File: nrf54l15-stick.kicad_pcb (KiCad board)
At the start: 4 copper layers, 14.5 x 22.5 mm, 29 parts, among them J1 USB_A, J2 programming conn, J3 Conn_01x04_Pin, SW4 SW_Push, SW5 SW_Push, SW6 Processor_reset, U3 APX803L20-29C3-7, U4 CP2102C-Axx-xQFN24, U5 BM15C, Y1 32.768kHz

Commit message: shrunk, routed, passes drc, no checklist yet
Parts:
- removed C4: 4.7uF/10V, Capacitor_SMD:C_0805_2012Metric
- removed J3: Conn_01x04_Pin, footprint:UART-sot
- removed SW5: SW_Push, footprint:SW_STU-057A23AC_8127_2.25N
- removed SW6: Processor_reset, footprint:SW_STU-057A23AC_8127_2.25N
- added C8: 4.7uF/10V, Capacitor_SMD:C_0603_1608Metric, B.Cu at (110.0, 95.2)
- added FID4: Fiducial, Fiducial:Fiducial_0.5mm_Mask1mm, B.Cu at (112.8, 86.4)
- added FID5: Fiducial, Fiducial:Fiducial_0.5mm_Mask1mm, B.Cu at (100.8, 86.4)
- added FID6: Fiducial, Fiducial:Fiducial_0.5mm_Mask1mm, B.Cu at (112.8, 95.4)
- C16: value 0.10uF/50V/0402 -> 0.10uF/50v
- C20: value 0.10uF/50V/0603 -> 0.10uF/50v; footprint Capacitor_SMD:C_0603_1608Metric -> Capacitor_SMD:C_0402_1005Metric
- C7: footprint Capacitor_SMD:C_0805_2012Metric -> Capacitor_SMD:C_0603_1608Metric
- D7, D8: footprint LED_SMD:LED_0805_2012Metric -> footprint:LED_0805_2012Metric; moved to B.Cu
- FID1, FID2, FID3: footprint Fiducial:Fiducial_1mm_Mask2mm -> Fiducial:Fiducial_0.5mm_Mask1mm
- H2, R16, SW4, Y1: moved to B.Cu
- R15: footprint Capacitor_SMD:C_0603_1608Metric -> Resistor_SMD:R_0603_1608Metric; moved to B.Cu
- R17: value 100K/0603 -> 100K; footprint Resistor_SMD:R_0603_1608Metric -> Resistor_SMD:R_0402_1005Metric
- R29: value 1.00K/0603 -> 1.00K; footprint Resistor_SMD:R_0603_1608Metric -> Resistor_SMD:R_0402_1005Metric
- R7: value 1k/0603 -> 1.00k; footprint Resistor_SMD:R_0603_1608Metric -> Resistor_SMD:R_0402_1005Metric
- R8: value 22.1k/0603 -> 22.1k; footprint Resistor_SMD:R_0603_1608Metric -> Resistor_SMD:R_0402_1005Metric
- R9: value 47.5k/0603 -> 47.5k; footprint Resistor_SMD:R_0603_1608Metric -> Resistor_SMD:R_0402_1005Metric
- U3: value APX803L20-29C3-7 -> APX803L20-27SR-7
- U4: footprint Package_DFN_QFN:WQFN-24-1EP_4x4mm_P0.5mm_EP2.45x2.45mm -> footprint:QFN-24-1EP_4x4mm_P0.5mm_EP2.5x2.5mm
- moved FID2 80.5 mm to (100.8, 93.0)
- moved C20 78.3 mm to (100.8, 92.2), turned to -90 degrees
- moved R17 77.0 mm to (101.8, 92.2), turned to 90 degrees
- moved SW4 74.7 mm to (101.4, 89.2), turned to 90 degrees
- moved U3 73.7 mm to (104.4, 90.8), turned to 180 degrees
- moved Z1 70.5 mm to (104.8, 95.6)
- moved D8 69.2 mm to (105.6, 87.8), turned to 90 degrees
- moved R7 67.9 mm to (102.8, 92.2), turned to 90 degrees
- moved Y1 67.4 mm to (104.8, 93.0)
- moved C16 66.7 mm to (101.6, 95.0)
- moved U5 66.5 mm to (106.8, 86.0)
- moved J2 66.4 mm to (106.8, 84.7)
- moved FID1 66.2 mm to (100.8, 84.6)
- moved R16 66.1 mm to (112.8, 93.0)
- moved R29 65.9 mm to (111.4, 87.2), turned to -90 degrees
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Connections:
- U4 pad 20: /UART_RX -> /UART_nRF_TX
- U4 pad 21: /UART_TX -> /UART_nRF_RX
- U5 pad A3: /P1.09 -> unconnected-(U5-P1.09-PadA3)
- U5 pad B3: /P1.11/AIN4 -> unconnected-(U5-P1.11/AIN4-PadB3)
- U5 pad B4: /P1.12/AIN5 -> unconnected-(U5-P1.12/AIN5-PadB4)
- U5 pad B5: /P1.13/AIN6 -> unconnected-(U5-P1.13/AIN6-PadB5)
- U5 pad B6: /P1.14/AIN7 -> unconnected-(U5-P1.14/AIN7-PadB6)
- U5 pad E8: /I2C_SDA -> unconnected-(U5-P1.03-PadE8)
- U5 pad E9: /I2C_SCL -> unconnected-(U5-P1.04/AIN0-PadE9)
- U5 pad F8: /UART_TX -> /UART_nRF_TX
- U5 pad F9: /UART_RX -> /UART_nRF_RX
- U5 pad G8: /PWM_CH_Y -> unconnected-(U5-P1.08-PadG8)
- U5 pad G9: /PWM_CH_X -> unconnected-(U5-P1.07/AIN3-PadG9)
- U5 pad J2: /BUTTON1 -> unconnected-(U5-P0.03-PadJ2)
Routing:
- net Net-(D8-A): track 2.20 -> 29.8 mm, vias 0 -> 2
- net /UART_RX: track 25.9 -> 0.00 mm, vias 3 -> 0
- net /BUTTON1: track 22.1 -> 0.00 mm, vias 2 -> 0
- net /UART_TX: track 16.0 -> 0.00 mm, vias 1 -> 0
- net Net-(U4-D-): track 0.00 -> 14.9 mm
- net Net-(D7-A): track 1.78 -> 15.1 mm, vias 0 -> 2
- net Net-(U4-VBUS): track 16.0 -> 3.06 mm, vias 2 -> 0
- net /UART_nRF_RX: track 0.00 -> 10.6 mm, vias 0 -> 1
- net Net-(U4-~{RST}): track 0.00 -> 9.52 mm
- net Net-(U4-D+): track 7.20 -> 15.1 mm, vias 0 -> 2
- net +5V: track 24.4 -> 16.9 mm
- net /UART_nRF_TX: track 0.00 -> 5.86 mm, vias 0 -> 1
- net /LED_BLUE: track 14.5 -> 19.4 mm, vias 0 -> 1
- net /P1.00/XTAL: track 6.89 -> 2.12 mm, vias 2 -> 1
- net /~{RESET}: track 17.8 -> 22.0 mm
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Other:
- board size 14.5 x 22.5 mm -> 13.6 x 17.2 mm
- board text removed: "G RX TX +V"

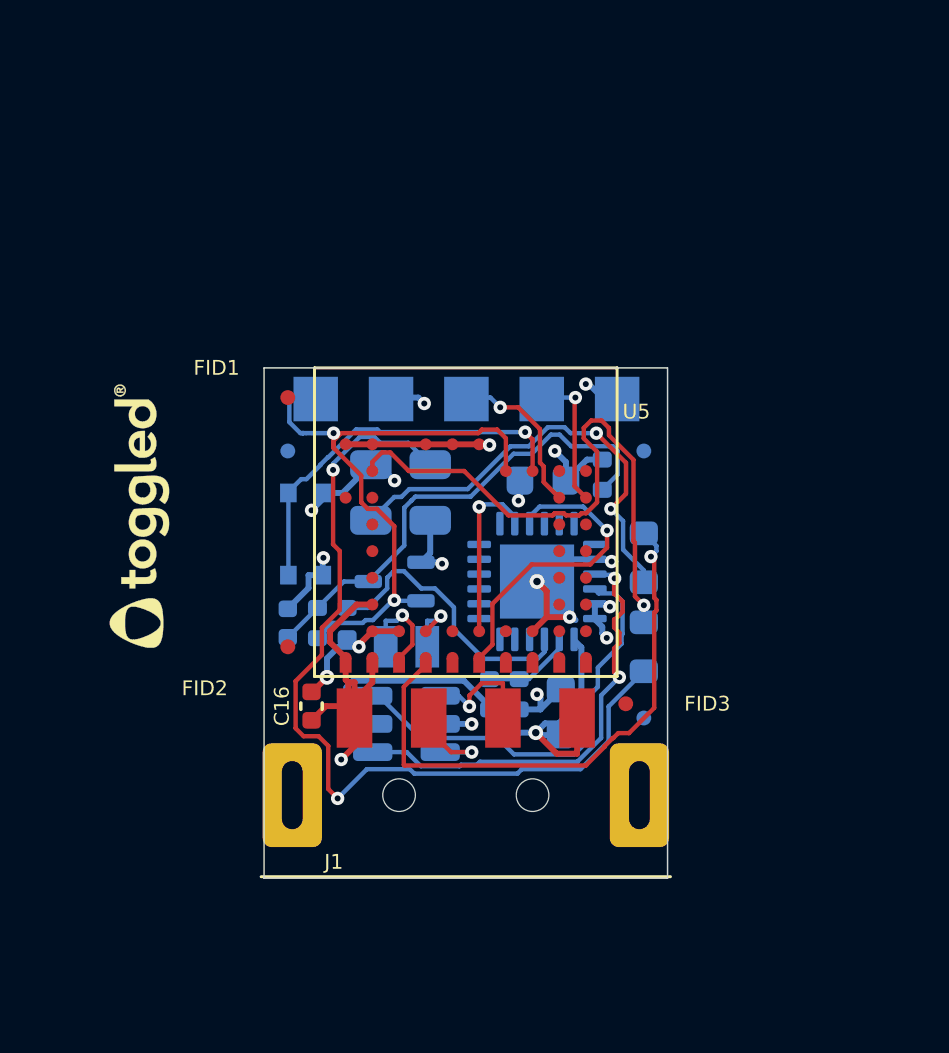
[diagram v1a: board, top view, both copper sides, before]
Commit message: fixed design net rules, passes drc
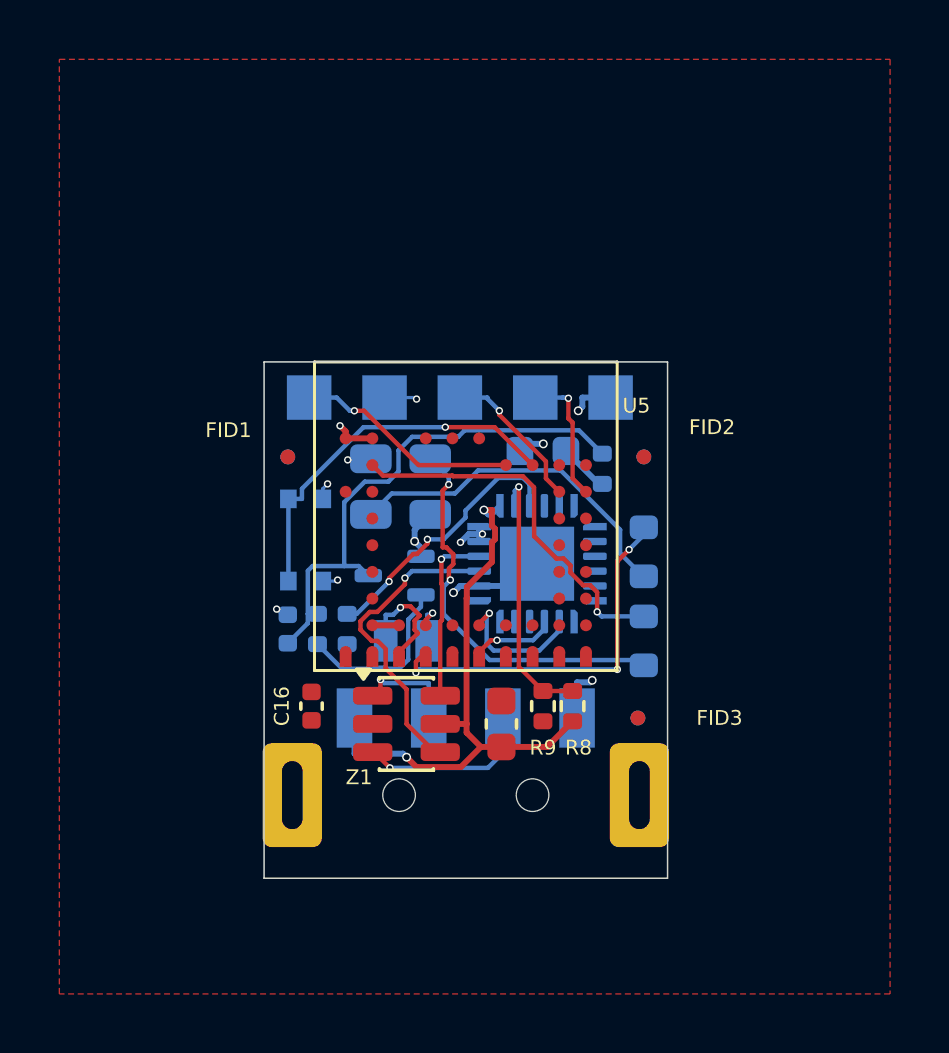
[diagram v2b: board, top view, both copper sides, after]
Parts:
- removed L1: toggled, footprint:toggled
- C8, R8, R9, Z1: moved to F.Cu
- J1: moved to B.Cu
- moved FID2 13.6 mm to (112.8, 86.6)
- moved H2 11.9 mm to (89.8, 92.2)
- moved R8 2.83 mm to (110.4, 95.0)
- moved C8 2.04 mm to (108.0, 95.6)
- moved FID1 2.00 mm to (100.8, 86.6)
- moved C7 1.00 mm to (109.4, 86.4)
- moved R9 0.89 mm to (109.4, 95.0)
- moved FID3 0.63 mm to (112.6, 95.4)
- moved U4 0.60 mm to (109.2, 90.2), turned to 0 degrees
- moved J2 0.23 mm to (106.6, 84.6)
- moved C20 0.20 mm to (100.8, 92.4)
- moved D7 0.20 mm to (103.6, 87.6)
- moved D8 0.20 mm to (105.6, 87.6)
- moved FID6 0.20 mm to (112.6, 95.4)
- moved R15 0.20 mm to (112.8, 89.8)
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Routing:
- net GND: track 36.3 -> 12.8 mm, vias 13 -> 10
- net Net-(D8-A): track 29.8 -> 13.4 mm
- net Net-(U4-D-): track 14.9 -> 5.95 mm, vias 0 -> 1
- net /~{RESET}: track 22.0 -> 13.5 mm, vias 2 -> 1
- net /UART_nRF_RX: track 10.6 -> 2.77 mm
- net /LED_RED: track 19.9 -> 12.8 mm
- net /LED_BLUE: track 19.4 -> 12.8 mm, vias 1 -> 3
- net Net-(U4-VBUS): track 3.06 -> 8.91 mm, vias 0 -> 1
- net Net-(U4-D+): track 15.1 -> 10.6 mm, vias 2 -> 1
- net VDD: track 9.88 -> 5.34 mm, vias 6 -> 3
- net Net-(D7-A): track 15.1 -> 11.8 mm, vias 2 -> 0
- net +5V: track 16.9 -> 19.9 mm, vias 1 -> 2
- net Net-(J1-D+): track 3.22 -> 5.99 mm
- net Net-(U3-VCC): track 16.4 -> 17.9 mm
- net /UART_nRF_TX: track 5.86 -> 4.73 mm
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- added copper zone on F.Cu, net GND
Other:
- board size 13.6 x 17.2 mm -> 13.6 x 17.4 mm
- board text added: "62-02454-AA 2026-06-23"
